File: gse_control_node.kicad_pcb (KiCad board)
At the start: 4 copper layers, 65 x 65 mm, 117 parts, among them J1 Screw_Terminal_01x02, J10 Conn_01x02, J2 Conn_01x04, J3 Conn_01x04, J4 Conn_02x01, J5 USB_C_Receptacle_USB2.0_16P, J6 Conn_01x04, J7 Conn_01x02, J8 Conn_01x02, J9 Conn_01x02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

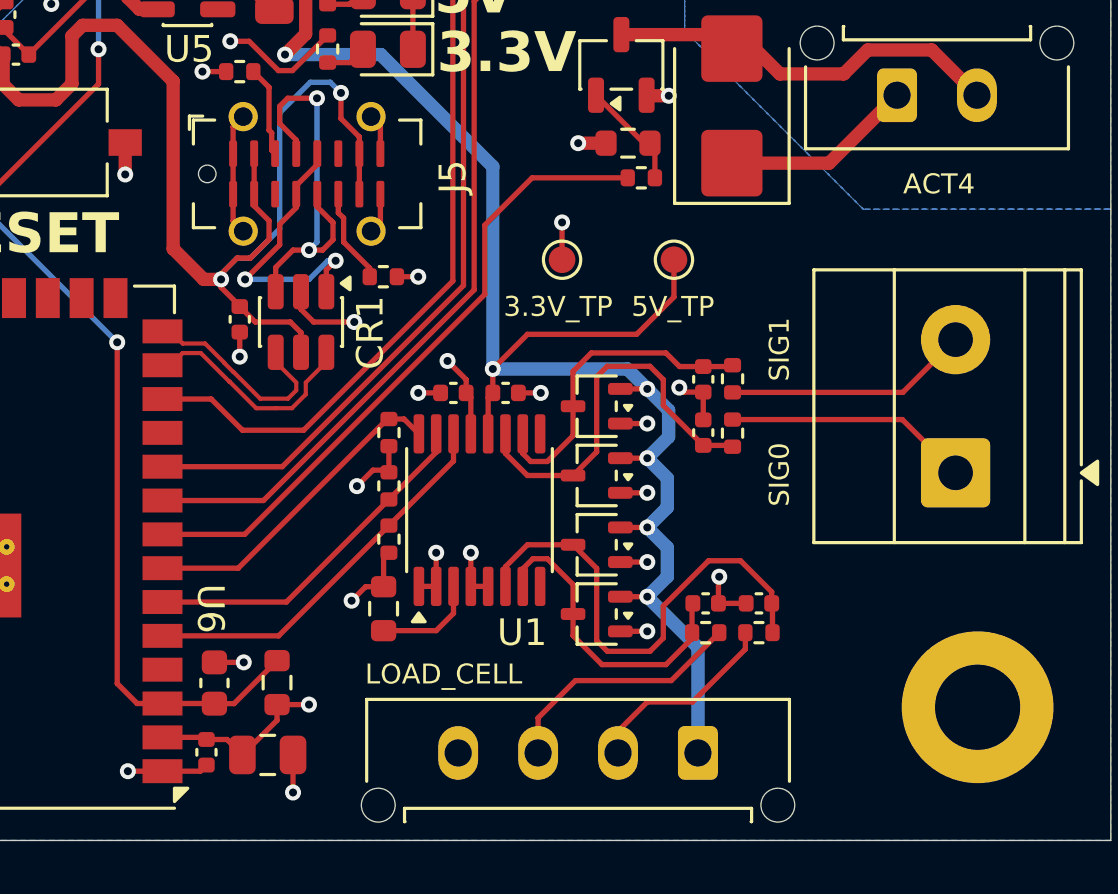
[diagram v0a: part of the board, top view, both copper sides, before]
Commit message: give more clearance for load cell connector from edge of board
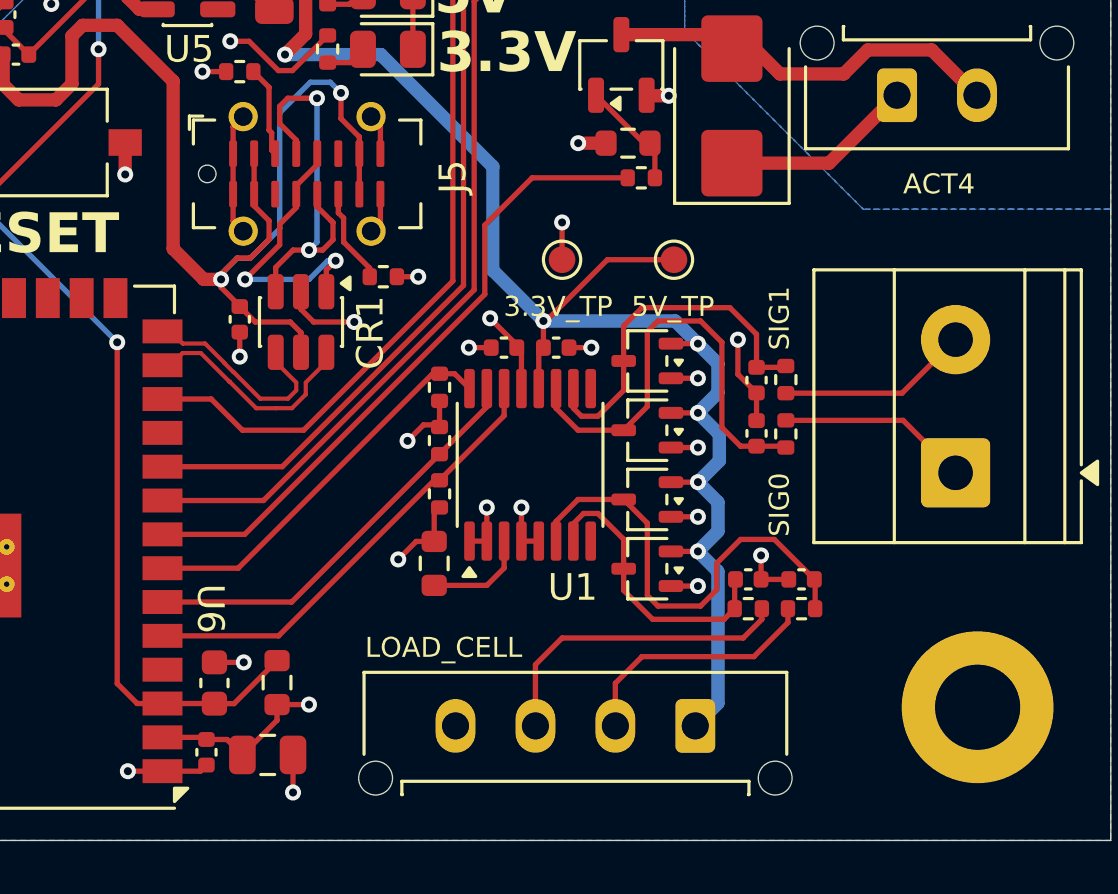
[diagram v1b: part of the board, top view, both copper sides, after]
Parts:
- moved C2 2.55 mm to (118.0, 74.3)
- moved U1 2.55 mm to (117.0, 78.7)
- moved C1 2.55 mm to (116.0, 74.3)
- moved D1 2.55 mm to (121.4, 80.0)
- moved D3 2.55 mm to (121.4, 82.6)
- moved D4 2.55 mm to (121.4, 74.8)
- moved D2 2.55 mm to (121.4, 77.4)
- moved R1 2.55 mm to (113.6, 79.8)
- moved R2 2.55 mm to (113.6, 75.8)
- moved R3 2.55 mm to (113.6, 77.8)
- moved R8 2.55 mm to (113.4, 82.4)
- moved C4 2.00 mm to (125.5, 77.5)
- moved C6 2.00 mm to (125.5, 75.5)
- moved R6 2.00 mm to (126.6, 75.5)
- moved R7 2.00 mm to (126.6, 77.5)
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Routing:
- net +5V: track 63.0 -> 59.3 mm
- net I2C_SCL: track 12.2 -> 14.8 mm
- net I2C_SDA: track 13.3 -> 15.9 mm
- net DRDY1: track 14.7 -> 17.3 mm
- net LOAD_CELL-: track 9.44 -> 11.9 mm
- net LOAD_CELL+: track 7.49 -> 9.54 mm
- net /ADC 1/AIN0: track 14.8 -> 16.8 mm
- net /ADC 1/SIG0: track 9.20 -> 7.19 mm
- net /ADC 1/SIG1: track 9.19 -> 7.21 mm
- net /ADC 1/AIN1: track 12.1 -> 13.5 mm
- net GND: track 81.3 -> 82.5 mm
- net /ADC 1/AIN3: track 18.5 -> 17.4 mm
- net /ADC 1/AIN2: track 11.7 -> 10.9 mm

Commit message: fix 5.17V buck switch node net name
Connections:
- net /Power Regulation/SW_5.3 renamed /Power Regulation/SW_5.17
- net /Power Regulation/VCC_5.3 renamed /Power Regulation/VCC_5.17
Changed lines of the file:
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@@
 			(layers "F.Cu" "F.Mask" "F.Paste")
 			(roundrect_rratio 0.25)
-			(net "/Power Regulation/VCC_5.3")
+			(net "/Power Regulation/VCC_5.17")
 			(pintype "passive")
 		)
@@
 			(layers "F.Cu" "F.Mask" "F.Paste")
 			(roundrect_rratio 0.25)
-			(net "/Power Regulation/SW_5.3")
+			(net "/Power Regulation/SW_5.17")
 			(pintype "passive")
 		)
@@
 			(size 2.95 3.5)
 			(layers "F.Cu" "F.Mask" "F.Paste")
-			(net "/Power Regulation/SW_5.3")
+			(net "/Power Regulation/SW_5.17")
 			(pintype "passive")
 		)
@@
 			(size 1.55 0.6)
 			(layers "F.Cu" "F.Mask" "F.Paste")
-			(net "/Power Regulation/VCC_5.3")
+			(net "/Power Regulation/VCC_5.17")
 			(pinfunction "VCC_6")
 			(pintype "power_out")
@@
 			(size 1.55 0.6)
 			(layers "F.Cu" "F.Mask" "F.Paste")
-			(net "/Power Regulation/SW_5.3")
+			(net "/Power Regulation/SW_5.17")
 			(pinfunction "SW_8")
 			(pintype "output")
@@
 	)
 	(segment
-		(start 113.185 44.95)
-		(end 113.185 42.99)
-		(width 0.5)
-		(layer "F.Cu")
-		(net "/Power Regulation/VCC_5.3")
-	)
-	(segment
-		(start 113.185 42.99)
-		(end 113.2 42.975)
-		(width 0.5)
-		(layer "F.Cu")
-		(net "/Power Regulation/VCC_5.3")
-	)
-	(segment
 		(start 116.166678 46.825)
 		(end 116.166678 47.8)
@@
 		(net "Net-(U1-RESET)")
 	)
+	(segment
+		(start 113.185 44.95)
+		(end 113.185 42.99)
+		(width 0.5)
+		(layer "F.Cu")
+		(net "/Power Regulation/VCC_5.17")
+	)
+	(segment
+		(start 113.185 42.99)
+		(end 113.2 42.975)
+		(width 0.5)
+		(layer "F.Cu")
+		(net "/Power Regulation/VCC_5.17")
+	)
 	(zone
 		(net "GND")
@@
 	)
 	(zone
-		(net "/Power Regulation/SW_5.3")
+		(net "/Power Regulation/SW_5.17")
 		(layer "F.Cu")
 		(hatch edge 0.5)

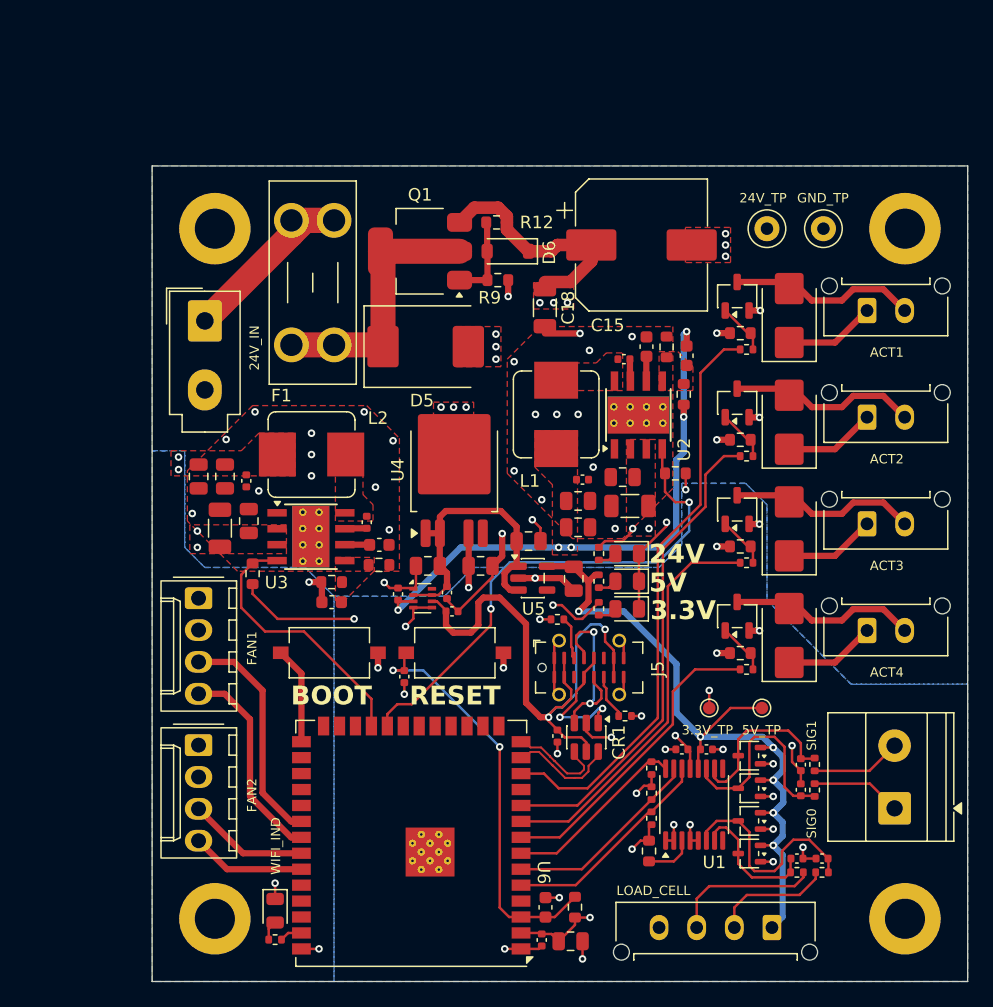
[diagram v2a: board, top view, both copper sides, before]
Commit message: switch to esp32-s3-wroom-1
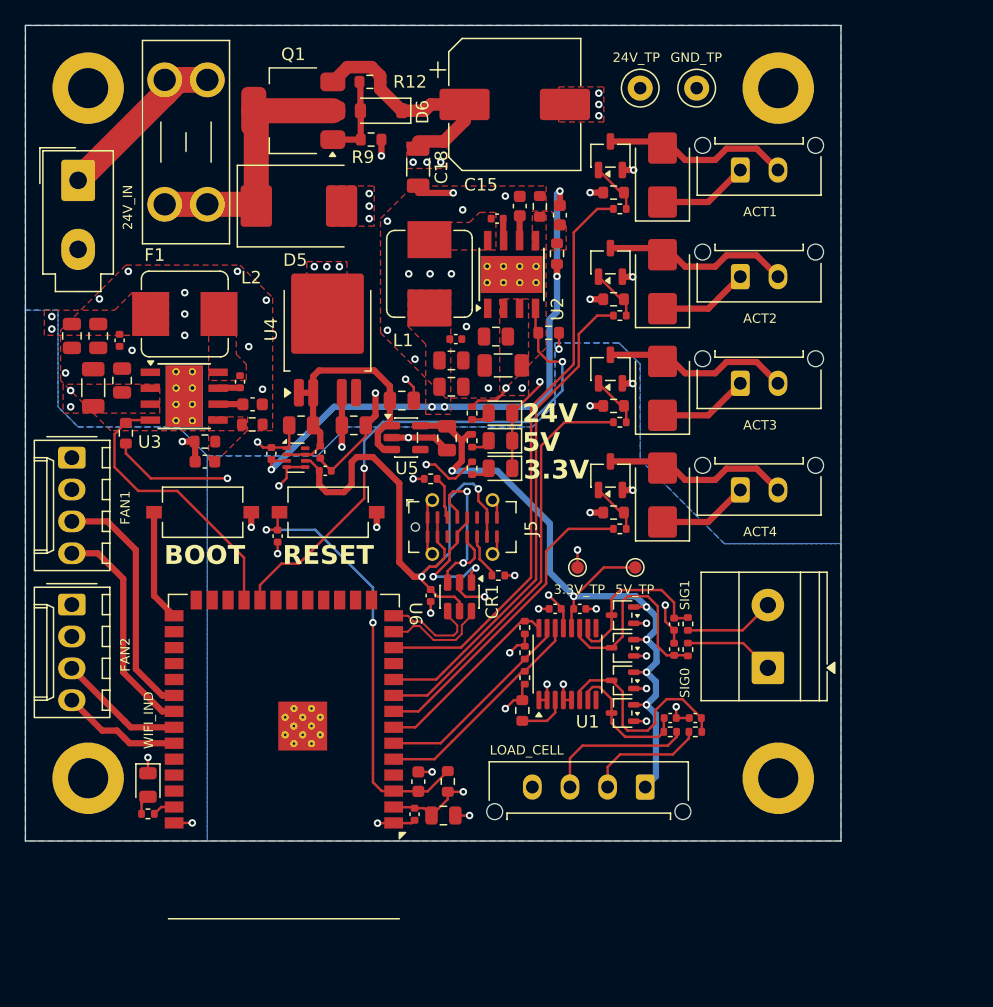
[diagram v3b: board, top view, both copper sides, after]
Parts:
- U6: value ESP32-S3-WROOM-1U -> ESP32-S3-WROOM-1; footprint RF_Module:ESP32-S3-WROOM-1U -> RF_Module:ESP32-S3-WROOM-1
- moved TP3 15.4 mm to (107.7, 59.8)
- moved C11 15.1 mm to (103.1, 31.0)
- moved C13 15.1 mm to (101.3, 32.0)
- moved C28 15.1 mm to (97.3, 49.5)
- moved C32 15.1 mm to (83.8, 57.3)
- moved C34 15.1 mm to (83.3, 50.7)
- moved C9 15.1 mm to (71.4, 44.9)
- moved CR1 15.1 mm to (98.3, 62.1)
- moved D11 15.1 mm to (114.5, 28.5)
- moved D12 15.1 mm to (114.5, 37.0)
- moved D13 15.1 mm to (114.5, 45.5)
- moved D6 15.1 mm to (92.0, 23.4)
- moved H4 15.1 mm to (123.7, 76.6)
- moved J10 15.1 mm to (120.7, 53.6)
- moved J3 15.1 mm to (113.1, 77.3)
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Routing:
- net /ESP32 Breakout/RESET: track 33.3 -> 35.3 mm
- net 5.17V_PG: track 41.2 -> 42.5 mm
- net FAN_1_TACH: track 18.3 -> 19.5 mm
- net FAN_1_PWM: track 16.5 -> 17.7 mm
- net 12V_PG: track 21.5 -> 22.6 mm
- net /ESP32 Breakout/BOOT: track 7.77 -> 8.91 mm
- net ACTUATOR_2_CTL: track 38.5 -> 39.0 mm
- net I2C_SCL: track 14.8 -> 15.3 mm
- net DRDY1: track 17.3 -> 17.8 mm
- net I2C_SDA: track 15.9 -> 16.4 mm
- net ACTUATOR_3_CTL: track 32.3 -> 32.9 mm
- net ACTUATOR_4_CTL: track 24.5 -> 25.1 mm
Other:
- board text added: "Footprint does not match as overhanging silkscreen lines were removed"

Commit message: update some routing and put ground pour on top layer to avoid warping
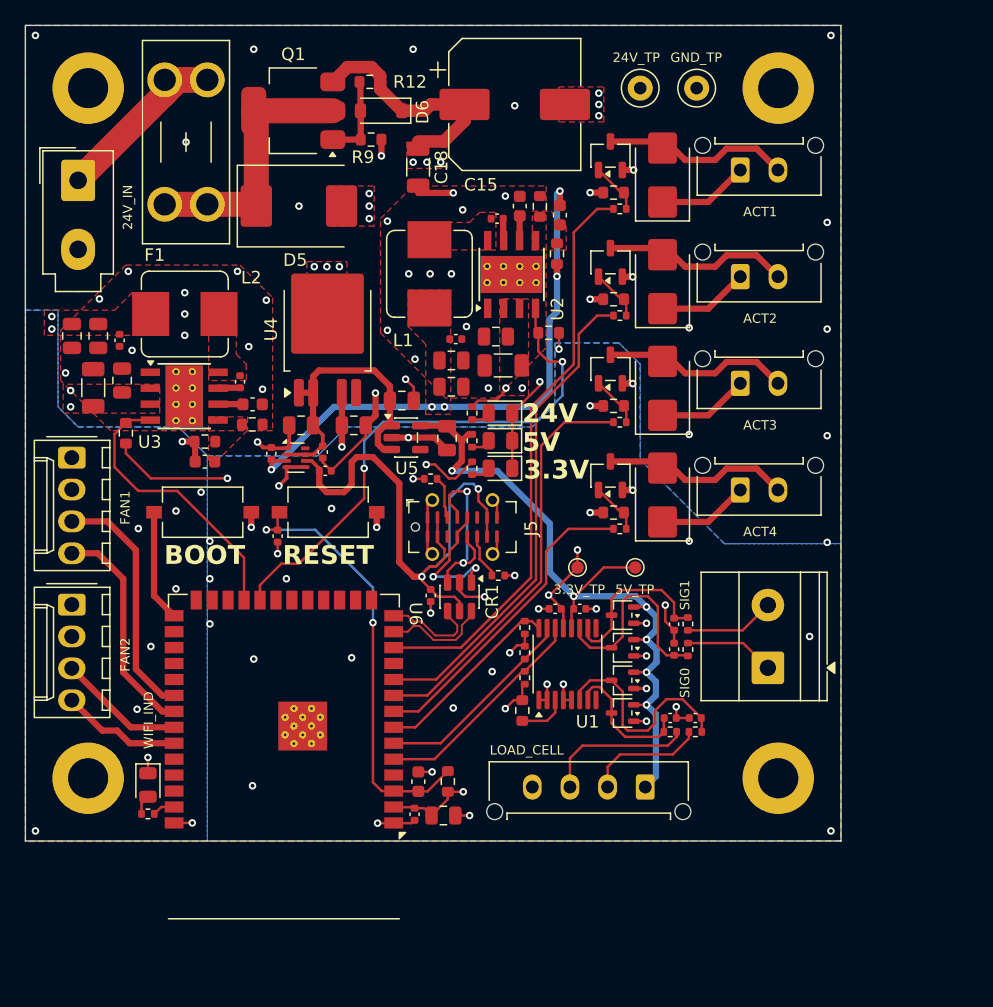
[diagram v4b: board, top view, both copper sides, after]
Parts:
- moved C36 0.20 mm to (87.4, 50.6)
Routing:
- net +3.3V: track 36.8 -> 40.1 mm
- net GND: track 82.3 -> 82.2 mm, vias 68 -> 101
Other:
- board text added: "Footprint does not match for DRC as overhanging silkscreen lines were removed"
- board text removed: "Footprint does not match as overhanging silkscreen lines were removed"

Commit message: update silkscreen
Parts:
- added G***: QRET_LOGO, LOGO, B.Cu at (96.9, 25.5)
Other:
- board text added: "5V + - GND"
- board text added: "D 24V"
- board text added: "GND 24V"
- board text added: "PWM TACH 12V GND"

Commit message: update all capacitors to jlcpcb basic components
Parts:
- C16, C17: value 3pF -> 10pF
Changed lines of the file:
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@@
 			)
 		)
-		(property "LCSC" "C85858"
+		(property "LCSC" "C307331"
 			(at 0 0 270)
 			(unlocked yes)
@@
 			)
 		)
-		(property "LCSC" "C85858"
+		(property "LCSC" "C307331"
 			(at 0 0 270)
 			(unlocked yes)
@@
 			)
 		)
-		(property "LCSC" "C29936"
+		(property "LCSC" "C15849"
 			(at 0 0 90)
 			(unlocked yes)
@@
 			)
 		)
-		(property "LCSC" "C85858"
+		(property "LCSC" "C307331"
 			(at 0 0 90)
 			(unlocked yes)
@@
 			)
 		)
-		(property "Value" "3pF"
+		(property "Value" "10pF"
 			(at 0 1.43 90)
 			(layer "F.Fab")
@@
 			)
 		)
-		(property "LCSC" "C162223"
+		(property "LCSC" "C1634"
 			(at 0 0 270)
 			(unlocked yes)
@@
 			)
 		)
-		(property "Value" "3pF"
+		(property "Value" "10pF"
 			(at 0 1.43 0)
 			(layer "F.Fab")
@@
 			)
 		)
-		(property "LCSC" "C162223"
+		(property "LCSC" "C1634"
 			(at 0 0 0)
 			(unlocked yes)
@@
 			)
 		)
-		(property "LCSC" "C85858"
+		(property "LCSC" "C307331"
 			(at 0 0 180)
 			(unlocked yes)
@@
 			)
 		)
-		(property "LCSC" "C77011"
+		(property "LCSC" "C16772"
 			(at 0 0 180)
 			(unlocked yes)
@@
 			)
 		)
-		(property "LCSC" "C29936"
+		(property "LCSC" "C15849"
 			(at 0 0 0)
 			(unlocked yes)
@@
 			)
 		)
-		(property "LCSC" "C77011"
+		(property "LCSC" "C16772"
 			(at 0 0 90)
 			(unlocked yes)
@@
 			)
 		)
-		(property "LCSC" "C85858"
+		(property "LCSC" "C307331"
 			(at 0 0 270)
 			(unlocked yes)
@@
 			)
 		)
-		(property "LCSC" "C85858"
+		(property "LCSC" "C307331"
 			(at 0 0 180)
 			(unlocked yes)
@@
 			)
 		)
-		(property "LCSC" "C85858"
+		(property "LCSC" "C307331"
 			(at 0 0 180)
 			(unlocked yes)
@@
 			)
 		)
-		(property "LCSC" "C77011"
+		(property "LCSC" "C16772"
 			(at 0 0 270)
 			(unlocked yes)
@@
 			)
 		)
-		(property "LCSC" "C85858"
+		(property "LCSC" "C307331"
 			(at 0 0 0)
 			(unlocked yes)
@@
 			)
 		)
-		(property "LCSC" "C85858"
+		(property "LCSC" "C307331"
 			(at 0 0 90)
 			(unlocked yes)
@@
 			)
 		)
-		(property "LCSC" "C85858"
+		(property "LCSC" "C307331"
 			(at 0 0 90)
 			(unlocked yes)
@@
 			)
 		)
-		(property "LCSC" "C29936"
+		(property "LCSC" "C15849"
 			(at 0 0 90)
 			(unlocked yes)
@@
 			)
 		)
-		(property "LCSC" "C85858"
+		(property "LCSC" "C307331"
 			(at 0 0 270)
 			(unlocked yes)
@@
 			)
 		)
-		(property "LCSC" "C77011"
+		(property "LCSC" "C16772"
 			(at 0 0 0)
 			(unlocked yes)
@@
 			)
 		)
-		(property "LCSC" "C85858"
+		(property "LCSC" "C307331"
 			(at 0 0 180)
 			(unlocked yes)

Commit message: add a 12v testpoint
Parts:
- added TP7: TP_+12V, TestPoint:TestPoint_Pad_D1.0mm, F.Cu at (65.5, 47.9)
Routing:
- net +24V: track 51.4 -> 32.5 mm
- net +12V: track 2.60 -> 4.20 mm, vias 3 -> 4
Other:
- board text added: "12V_TP"
